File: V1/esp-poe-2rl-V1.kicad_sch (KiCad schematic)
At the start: 56 parts, among them J1 USB_C_Receptacle_USB2.0, J2 RJ45 JACK, J3 1x2P 5,08mm, J4 1x2P 5,08mm, K1 Songle SRD-5VDC-SL-A, K2 Songle SRD-5VDC-SL-A, Q1 UMH3N, Q2 WPM2015-3/TR, Q3 LMUN2211LT1G, Q4 MMBT2222A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

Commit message: Layouting
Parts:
- J1: footprint Tales:USB_C_Receptacle_JAE_DX07S024WJ1R350 -> Tales:USB_C_Receptacle_GCT_USB4105-xx-A_16P_TopMnt_Horizontal; symbol Connector:USB_C_Receptacle_USB2.0 -> Tales:USB_C_Receptacle_USB2.0; LCSC Part # C3001281 -> C2765186; Mfr G-Switch -> Shou Han; Mfr PN GT-USB-7028D -> TYPE-C 16PIN 2MD(073); Vendor PN C3001281 -> C2765186
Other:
- note added: "CONECTOR ORIGINAL DO PROJETO: C3001281 VERTICAL FOOTPRINT ORIGINAL: Tales:USB_C_Receptacle_JAE_DX07S024WJ1R350 SUBSTITUÍDO POR: C2765186 HORIZONTAL FOOTPRINT: Tales:USB_C_Receptacle_GCT_USB4105-xx-A_16P_TopMnt_Horizontal"
- note removed: "SUBSTITUIR POR C2765186"
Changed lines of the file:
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@@
   (junction (at 387.35 144.78) (diameter 0) (color 0 0 0 0)
   )
+  (junction (at 59.69 48.26) (diameter 0) (color 0 0 0 0)
+  )
   (junction (at 128.27 190.5) (diameter 0) (color 0 0 0 0)
   )
@@
   (junction (at 293.37 187.96) (diameter 0) (color 0 0 0 0)
   )
+  (junction (at 59.69 50.8) (diameter 0) (color 0 0 0 0)
+  )
   (junction (at 250.19 46.99) (diameter 0) (color 0 0 0 0)
   )
@@
   (junction (at 316.23 46.99) (diameter 0) (color 0 0 0 0)
   )
+  (junction (at 59.69 45.72) (diameter 0) (color 0 0 0 0)
+  )
   (junction (at 59.69 71.12) (diameter 0) (color 0 0 0 0)
   )
@@
     (stroke (width 0) (type default))
   )
+  (wire (pts (xy 57.15 48.26) (xy 59.69 48.26))
+    (stroke (width 0) (type default))
+  )
   (wire (pts (xy 128.27 247.65) (xy 128.27 248.92))
     (stroke (width 0) (type default))
@@
     (stroke (width 0) (type default))
   )
+  (wire (pts (xy 57.15 50.8) (xy 59.69 50.8))
+    (stroke (width 0) (type default))
+  )
   (wire (pts (xy 143.51 238.76) (xy 144.78 238.76))
     (stroke (width 0) (type default))
@@
     (stroke (width 0) (type default))
   )
-  (wire (pts (xy 59.69 40.64) (xy 59.69 53.34))
+  (wire (pts (xy 59.69 40.64) (xy 59.69 45.72))
     (stroke (width 0) (type default))
   )
@@
     (stroke (width 0) (type default))
   )
+  (wire (pts (xy 59.69 45.72) (xy 59.69 48.26))
+    (stroke (width 0) (type default))
+  )
   (wire (pts (xy 309.88 214.63) (xy 351.79 214.63))
     (stroke (width 0) (type default))
@@
     (stroke (width 0) (type default))
   )
+  (wire (pts (xy 59.69 48.26) (xy 59.69 50.8))
+    (stroke (width 0) (type default))
+  )
   (wire (pts (xy 152.4 228.6) (xy 152.4 232.41))
     (stroke (width 0) (type default))
@@
     (stroke (width 0) (type default))
   )
+  (wire (pts (xy 59.69 50.8) (xy 59.69 53.34))
+    (stroke (width 0) (type default))
+  )
   (wire (pts (xy 288.29 187.96) (xy 293.37 187.96))
     (stroke (width 0) (type default))
@@
     (stroke (width 0) (type default))
   )
+  (wire (pts (xy 57.15 45.72) (xy 59.69 45.72))
+    (stroke (width 0) (type default))
+  )
   (wire (pts (xy 115.57 78.74) (xy 115.57 83.82))
     (stroke (width 0) (type default))
@@
     (effects (font (size 1.27 1.27)) (justify left bottom))
   )
-  (text "SUBSTITUIR POR C2765186" (at 29.21 101.6 0)
+  (text "CONECTOR ORIGINAL DO PROJETO: C3001281 VERTICAL\nFOOTPRINT ORIGINAL: Tales:USB_C_Receptacle_JAE_DX07S024WJ1R350\nSUBSTITUÍDO POR: C2765186 HORIZONTAL\nFOOTPRINT: Tales:USB_C_Receptacle_GCT_USB4105-xx-A_16P_TopMnt_Horizontal"
+    (at 30.48 106.68 0)
     (effects (font (size 1.27 1.27)) (justify left bottom))
   )
@@
     )
   )
-  (symbol (lib_id "Connector:USB_C_Receptacle_USB2.0") (at 41.91 68.58 0) (unit 1)
-    (in_bom yes) (on_board yes) (dnp no)
-    (property "Reference" "J1" (at 41.91 44.45 0)
+  (symbol (lib_id "Tales:USB_C_Receptacle_USB2.0") (at 41.91 63.5 0) (unit 1)
+    (in_bom yes) (on_board yes) (dnp no) (fields_autoplaced)
+    (property "Reference" "J1" (at 41.91 36.83 0)
       (effects (font (size 1.27 1.27)))
     )
-    (property "Value" "USB_C_Receptacle_USB2.0" (at 41.91 46.99 0)
+    (property "Value" "USB_C_Receptacle_USB2.0" (at 41.91 39.37 0)
       (effects (font (size 1.27 1.27)))
     )
-    (property "Footprint" "Tales:USB_C_Receptacle_JAE_DX07S024WJ1R350" (at 45.72 68.58 0)
+    (property "Footprint" "Tales:USB_C_Receptacle_GCT_USB4105-xx-A_16P_TopMnt_Horizontal" (at 45.72 63.5 0)
       (effects (font (size 1.27 1.27)) hide)
     )
-    (property "Datasheet" "~" (at 45.72 68.58 0)
+    (property "Datasheet" "~" (at 45.72 63.5 0)
       (effects (font (size 1.27 1.27)) hide)
     )
-    (property "Case" "~" (at 41.91 68.58 0)
+    (property "Case" "~" (at 41.91 63.5 0)
       (effects (font (size 1.27 1.27)) hide)
     )
-    (property "JLCPCB BOM" "1" (at 41.91 68.58 0)
+    (property "JLCPCB BOM" "1" (at 41.91 63.5 0)
       (effects (font (size 1.27 1.27)) hide)
     )
-    (property "LCSC Part #" "C3001281" (at 41.91 49.53 0)
+    (property "LCSC Part #" "C2765186" (at 41.91 41.91 0)
       (effects (font (size 1.27 1.27)))
     )
-    (property "Mfr" "G-Switch" (at 41.91 68.58 0)
+    (property "Mfr" "Shou Han" (at 41.91 63.5 0)
       (effects (font (size 1.27 1.27)) hide)
     )
-    (property "Mfr PN" "GT-USB-7028D" (at 41.91 68.58 0)
+    (property "Mfr PN" "TYPE-C 16PIN 2MD(073)" (at 41.91 63.5 0)
       (effects (font (size 1.27 1.27)) hide)
     )
-    (property "Technology" "~" (at 41.91 68.58 0)
+    (property "Technology" "~" (at 41.91 63.5 0)
       (effects (font (size 1.27 1.27)) hide)
     )
-    (property "Vendor" "JLCPCB" (at 41.91 68.58 0)
+    (property "Vendor" "JLCPCB" (at 41.91 63.5 0)
       (effects (font (size 1.27 1.27)) hide)
     )
-    (property "Vendor PN" "C3001281" (at 41.91 68.58 0)
+    (property "Vendor PN" "C2765186" (at 41.91 63.5 0)
       (effects (font (size 1.27 1.27)) hide)
     )

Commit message: Replace power connectors
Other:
- note added: "TROCAR CONECTORES POR HORIZONTAL C2898709"
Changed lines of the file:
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@@
+    (effects (font (size 1.27 1.27)) (justify left bottom))
+  )
+  (text "TROCAR CONECTORES POR HORIZONTAL\nC2898709" (at 203.2 179.07 0)
     (effects (font (size 1.27 1.27)) (justify left bottom))
   )

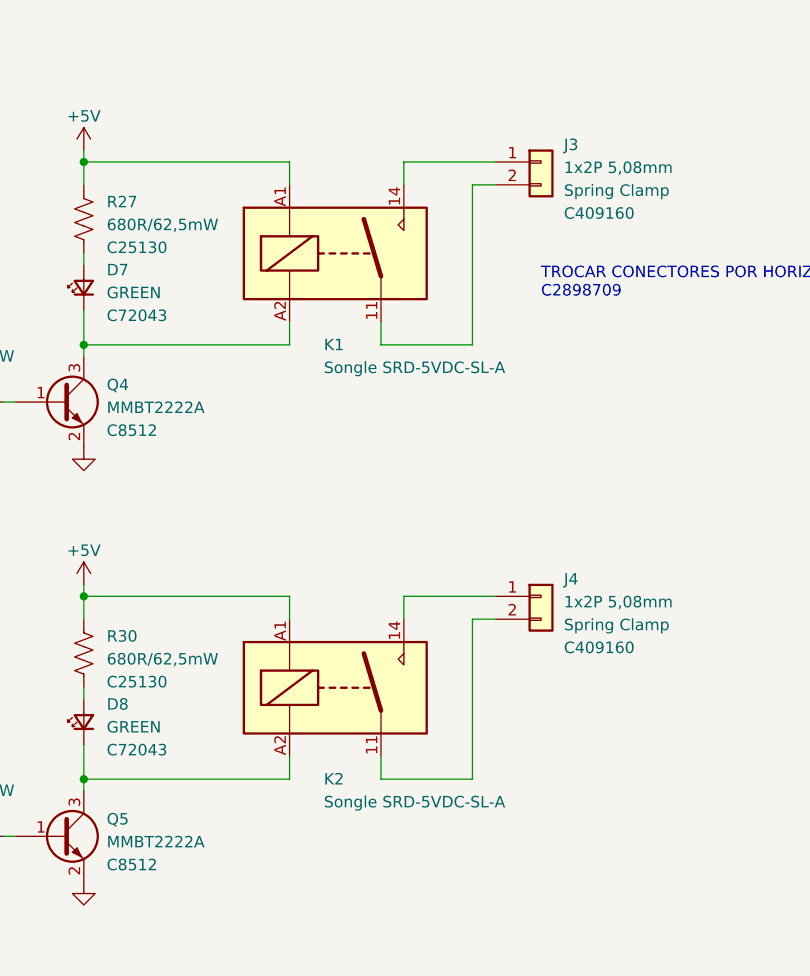
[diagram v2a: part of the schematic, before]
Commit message: Replaced relays
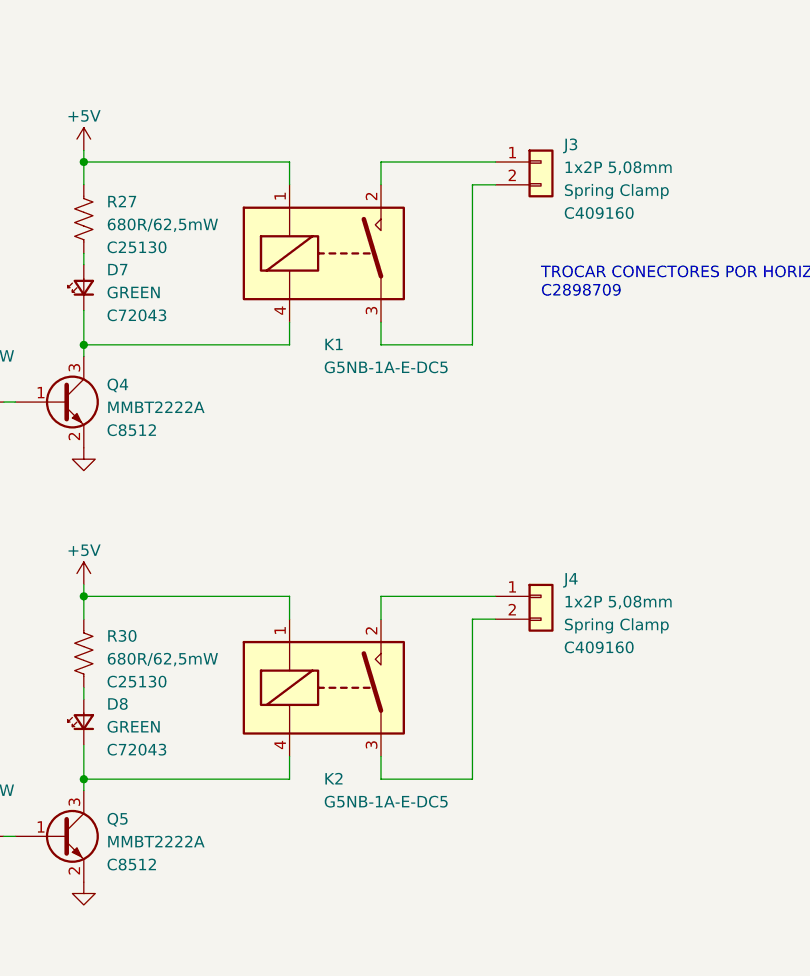
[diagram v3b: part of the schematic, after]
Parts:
- K1, K2: value Songle SRD-5VDC-SL-A -> G5NB-1A-E-DC5; footprint Tales:Relay_SPST_Songle_SRD_FormA -> Tales:Relay_SPST_Omron_G5NB-1A; symbol Tales:Songle_SRD -> Tales:G5NZ-1A; Case SPST Form A -> (none); LCSC Part # C140615 -> C48746; Mfr Songle -> Omron; Mfr PN SRD-05VDC-SL-A -> G5NB-1A-E-DC5; Vendor PN C140615 -> C48746
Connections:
- net +5V: now also K1.1, K2.1; no longer K1.A1, K2.A1
- net at D8.1 (K), Q5.3 (C): now also K2.4; no longer K2.A2
- net at D7.1 (K), Q4.3 (C): now also K1.4; no longer K1.A2
- net at J3.2 (Pin_2): now also K1.3; no longer K1.11
- net at J3.1 (Pin_1): now also K1.2; no longer K1.14
- net at J4.1 (Pin_1): now also K2.2; no longer K2.14
- net at J4.2 (Pin_2): now also K2.3; no longer K2.11
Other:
- moved on the sheet: K1, K2
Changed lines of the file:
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@@
     (stroke (width 0) (type default))
   )
-  (wire (pts (xy 198.12 212.09) (xy 187.96 212.09))
+  (wire (pts (xy 198.12 212.09) (xy 185.42 212.09))
     (stroke (width 0) (type default))
   )
@@
     (stroke (width 0) (type default))
   )
-  (wire (pts (xy 187.96 163.83) (xy 187.96 166.37))
+  (wire (pts (xy 185.42 163.83) (xy 185.42 166.37))
     (stroke (width 0) (type default))
   )
@@
     (stroke (width 0) (type default))
   )
-  (wire (pts (xy 187.96 212.09) (xy 187.96 214.63))
+  (wire (pts (xy 185.42 212.09) (xy 185.42 214.63))
     (stroke (width 0) (type default))
   )
@@
     (stroke (width 0) (type default))
   )
-  (wire (pts (xy 198.12 163.83) (xy 187.96 163.83))
+  (wire (pts (xy 198.12 163.83) (xy 185.42 163.83))
     (stroke (width 0) (type default))
   )
@@
     )
   )
-  (symbol (lib_id "Tales:Songle_SRD") (at 180.34 173.99 0) (unit 1)
+  (symbol (lib_id "Tales:G5NZ-1A") (at 180.34 173.99 0) (unit 1)
     (in_bom yes) (on_board yes) (dnp no)
     (property "Reference" "K1" (at 179.07 184.15 0)
       (effects (font (size 1.27 1.27)) (justify left))
     )
-    (property "Value" "Songle SRD-5VDC-SL-A" (at 179.07 186.69 0)
+    (property "Value" "G5NB-1A-E-DC5" (at 179.07 186.69 0)
       (effects (font (size 1.27 1.27)) (justify left))
     )
-    (property "Footprint" "Tales:Relay_SPST_Songle_SRD_FormA" (at 209.296 175.006 0)
-      (effects (font (size 1.27 1.27)) hide)
+    (property "Footprint" "Tales:Relay_SPST_Omron_G5NB-1A" (at 189.23 175.26 0)
+      (effects (font (size 1.27 1.27)) (justify left) hide)
     )
     (property "Datasheet" "~" (at 180.34 173.99 0)
       (effects (font (size 1.27 1.27)) hide)
     )
-    (property "Case" "SPST Form A" (at 180.34 173.99 0)
+    (property "Case" "~" (at 180.34 173.99 0)
       (effects (font (size 1.27 1.27)) hide)
     )
@@
       (effects (font (size 1.27 1.27)) hide)
     )
-    (property "LCSC Part #" "C140615" (at 180.34 173.99 0)
+    (property "LCSC Part #" "C48746" (at 180.34 173.99 0)
       (effects (font (size 1.27 1.27)) hide)
     )
-    (property "Mfr" "Songle" (at 180.34 173.99 0)
+    (property "Mfr" "Omron" (at 180.34 173.99 0)
       (effects (font (size 1.27 1.27)) hide)
     )
-    (property "Mfr PN" "SRD-05VDC-SL-A" (at 180.34 173.99 0)
+    (property "Mfr PN" "G5NB-1A-E-DC5" (at 180.34 173.99 0)
       (effects (font (size 1.27 1.27)) hide)
     )
@@
       (effects (font (size 1.27 1.27)) hide)
     )
-    (property "Vendor PN" "C140615" (at 180.34 173.99 0)
+    (property "Vendor PN" "C48746" (at 180.34 173.99 0)
       (effects (font (size 1.27 1.27)) hide)
     )
-    (pin "11")
-    (pin "14")
-    (pin "A1")
-    (pin "A2")
+    (pin "1")
+    (pin "2")
+    (pin "3")
+    (pin "4")
     (instances
       (project "esp-poe-2rl-V1"
@@
     )
   )
-  (symbol (lib_id "Tales:Songle_SRD") (at 180.34 222.25 0) (unit 1)
+  (symbol (lib_id "Tales:G5NZ-1A") (at 180.34 222.25 0) (unit 1)
     (in_bom yes) (on_board yes) (dnp no) (fields_autoplaced)
     (property "Reference" "K2" (at 179.07 232.41 0)
       (effects (font (size 1.27 1.27)) (justify left))
     )
-    (property "Value" "Songle SRD-5VDC-SL-A" (at 179.07 234.95 0)
+    (property "Value" "G5NB-1A-E-DC5" (at 179.07 234.95 0)
       (effects (font (size 1.27 1.27)) (justify left))
     )
-    (property "Footprint" "Tales:Relay_SPST_Songle_SRD_FormA" (at 209.296 223.266 0)
-      (effects (font (size 1.27 1.27)) hide)
+    (property "Footprint" "Tales:Relay_SPST_Omron_G5NB-1A" (at 189.23 223.52 0)
+      (effects (font (size 1.27 1.27)) (justify left) hide)
     )
     (property "Datasheet" "~" (at 180.34 222.25 0)
       (effects (font (size 1.27 1.27)) hide)
     )
-    (property "Case" "SPST Form A" (at 180.34 222.25 0)
+    (property "Case" "~" (at 180.34 222.25 0)
       (effects (font (size 1.27 1.27)) hide)
     )
@@
       (effects (font (size 1.27 1.27)) hide)
     )
-    (property "LCSC Part #" "C140615" (at 180.34 222.25 0)
+    (property "LCSC Part #" "C48746" (at 180.34 222.25 0)
       (effects (font (size 1.27 1.27)) hide)
     )
-    (property "Mfr" "Songle" (at 180.34 222.25 0)
+    (property "Mfr" "Omron" (at 180.34 222.25 0)
       (effects (font (size 1.27 1.27)) hide)
     )
-    (property "Mfr PN" "SRD-05VDC-SL-A" (at 180.34 222.25 0)
+    (property "Mfr PN" "G5NB-1A-E-DC5" (at 180.34 222.25 0)
       (effects (font (size 1.27 1.27)) hide)
     )
@@
       (effects (font (size 1.27 1.27)) hide)
     )
-    (property "Vendor PN" "C140615" (at 180.34 222.25 0)
+    (property "Vendor PN" "C48746" (at 180.34 222.25 0)
       (effects (font (size 1.27 1.27)) hide)
     )
-    (pin "11")
-    (pin "14")
-    (pin "A1")
-    (pin "A2")
+    (pin "1")
+    (pin "2")
+    (pin "3")
+    (pin "4")
     (instances
       (project "esp-poe-2rl-V1"

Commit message: Updating
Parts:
- J3, J4: footprint Tales:TerminalBlock_JL142V-5.08-2P_1x02_P5.08mm_Vertical -> Tales:TerminalBlock_Dibo_DB142V-2-5.08_1x02_P5.08mm_Vertical
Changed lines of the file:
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@@
       (effects (font (size 1.27 1.27)) (justify left))
     )
-    (property "Footprint" "Tales:TerminalBlock_JL142V-5.08-2P_1x02_P5.08mm_Vertical" (at 203.2 212.09 0)
+    (property "Footprint" "Tales:TerminalBlock_Dibo_DB142V-2-5.08_1x02_P5.08mm_Vertical" (at 203.2 212.09 0)
       (effects (font (size 1.27 1.27)) hide)
     )
@@
       (effects (font (size 1.27 1.27)) (justify left))
     )
-    (property "Footprint" "Tales:TerminalBlock_JL142V-5.08-2P_1x02_P5.08mm_Vertical" (at 203.2 163.83 0)
-      (effects (font (size 1.27 1.27)) hide)
-    )
+    (property "Footprint" "Tales:TerminalBlock_Dibo_DB142V-2-5.08_1x02_P5.08mm_Vertical" (at 203.2 163.83 0)
+      (effects (font (size 1.27 1.27)) hide)
+    )

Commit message: Layout optimization
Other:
- note added: "TROCAR CH340C POR CH340T SSOP20"
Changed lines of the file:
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@@
     (stroke (width 0) (type default))
+  )
+  (text "TROCAR CH340C POR CH340T SSOP20" (at 77.47 121.92 0)
+    (effects (font (size 1.27 1.27)) (justify left bottom))
   )
   (text "ESP32 PIN ASSIGNMENT\n25 - GPIO0 - AUTO FLASH MODE\n35 - GPIO1 - SERIAL TX\n34 - GPIO3 - SERIAL RX\n14 - GPIO12 - PHY POWER\n16 - GPIO13 - MCP23017 INTA\n13 - GPIO14 - MCP23017 INTB\n28 - GPIO17 - EMAC CLK\n30 - GPIO18 - EMAC MDIO\n31 - GPIO19 - EMAC TXD0\n33 - GPIO21 - EMAC TXEN\n36 - GPIO22 - EMAC TXD1\n37 - GPIO23 - EMAC MDC\n10 - GPIO25 - EMAC RXD0\n11 - GPIO26 - EMAC RXD1\n12 - GPIO27 - EMAC RX\n8 - GPIO32 - I2C SCL\n9 - GPIO33 - I2C SDA"

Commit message: PCB shrinking process
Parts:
- J3, J4: footprint Tales:TerminalBlock_Dibo_DB142V-2-5.08_1x02_P5.08mm_Vertical -> Tales:TerminalBlock_Dibo_DB142R-2-5.08_1x02_P5.08mm_Horizontal; LCSC Part # C409160 -> C2898709; Mfr JILN -> Dibo; Mfr PN JL142V-50802GA1 -> DB142R-5.08-2P; Vendor PN C409160 -> C2898709
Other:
- note removed: "TROCAR CONECTORES POR HORIZONTAL C2898709"
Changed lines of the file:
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@@
     (effects (font (size 1.27 1.27)) (justify left bottom))
   )
-  (text "TROCAR CONECTORES POR HORIZONTAL\nC2898709" (at 203.2 179.07 0)
-    (effects (font (size 1.27 1.27)) (justify left bottom))
-  )
   (label "EMAC_RX" (at 200.66 113.03 0) (fields_autoplaced)
     (effects (font (size 1.27 1.27)) (justify left bottom))
@@
       (effects (font (size 1.27 1.27)) (justify left))
     )
-    (property "Footprint" "Tales:TerminalBlock_Dibo_DB142V-2-5.08_1x02_P5.08mm_Vertical" (at 203.2 212.09 0)
+    (property "Footprint" "Tales:TerminalBlock_Dibo_DB142R-2-5.08_1x02_P5.08mm_Horizontal" (at 203.2 212.09 0)
       (effects (font (size 1.27 1.27)) hide)
     )
@@
       (effects (font (size 1.27 1.27)) (justify left))
     )
-    (property "LCSC Part #" "C409160" (at 205.74 217.805 0)
+    (property "LCSC Part #" "C2898709" (at 205.74 217.805 0)
       (effects (font (size 1.27 1.27)) (justify left))
     )
-    (property "Mfr" "JILN" (at 203.2 212.09 0)
+    (property "Mfr" "Dibo" (at 203.2 212.09 0)
       (effects (font (size 1.27 1.27)) hide)
     )
-    (property "Mfr PN" "JL142V-50802GA1" (at 203.2 212.09 0)
+    (property "Mfr PN" "DB142R-5.08-2P" (at 203.2 212.09 0)
       (effects (font (size 1.27 1.27)) hide)
     )
@@
       (effects (font (size 1.27 1.27)) hide)
     )
-    (property "Vendor PN" "C409160" (at 203.2 212.09 0)
+    (property "Vendor PN" "C2898709" (at 203.2 212.09 0)
       (effects (font (size 1.27 1.27)) hide)
     )
@@
       (effects (font (size 1.27 1.27)) (justify left))
     )
-    (property "Footprint" "Tales:TerminalBlock_Dibo_DB142V-2-5.08_1x02_P5.08mm_Vertical" (at 203.2 163.83 0)
+    (property "Footprint" "Tales:TerminalBlock_Dibo_DB142R-2-5.08_1x02_P5.08mm_Horizontal" (at 203.2 163.83 0)
       (effects (font (size 1.27 1.27)) hide)
     )
@@
       (effects (font (size 1.27 1.27)) (justify left))
     )
-    (property "LCSC Part #" "C409160" (at 205.74 169.545 0)
+    (property "LCSC Part #" "C2898709" (at 205.74 169.545 0)
       (effects (font (size 1.27 1.27)) (justify left))
     )
-    (property "Mfr" "JILN" (at 203.2 163.83 0)
+    (property "Mfr" "Dibo" (at 203.2 163.83 0)
       (effects (font (size 1.27 1.27)) hide)
     )
-    (property "Mfr PN" "JL142V-50802GA1" (at 203.2 163.83 0)
+    (property "Mfr PN" "DB142R-5.08-2P" (at 203.2 163.83 0)
       (effects (font (size 1.27 1.27)) hide)
     )
@@
       (effects (font (size 1.27 1.27)) hide)
     )
-    (property "Vendor PN" "C409160" (at 203.2 163.83 0)
+    (property "Vendor PN" "C2898709" (at 203.2 163.83 0)
       (effects (font (size 1.27 1.27)) hide)
     )
